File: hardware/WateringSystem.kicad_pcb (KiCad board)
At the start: 4 copper layers, 70 x 66 mm, 3 parts, among them IC1 MAX485ESA+T, U1 ESP32-DEVKITC-32E

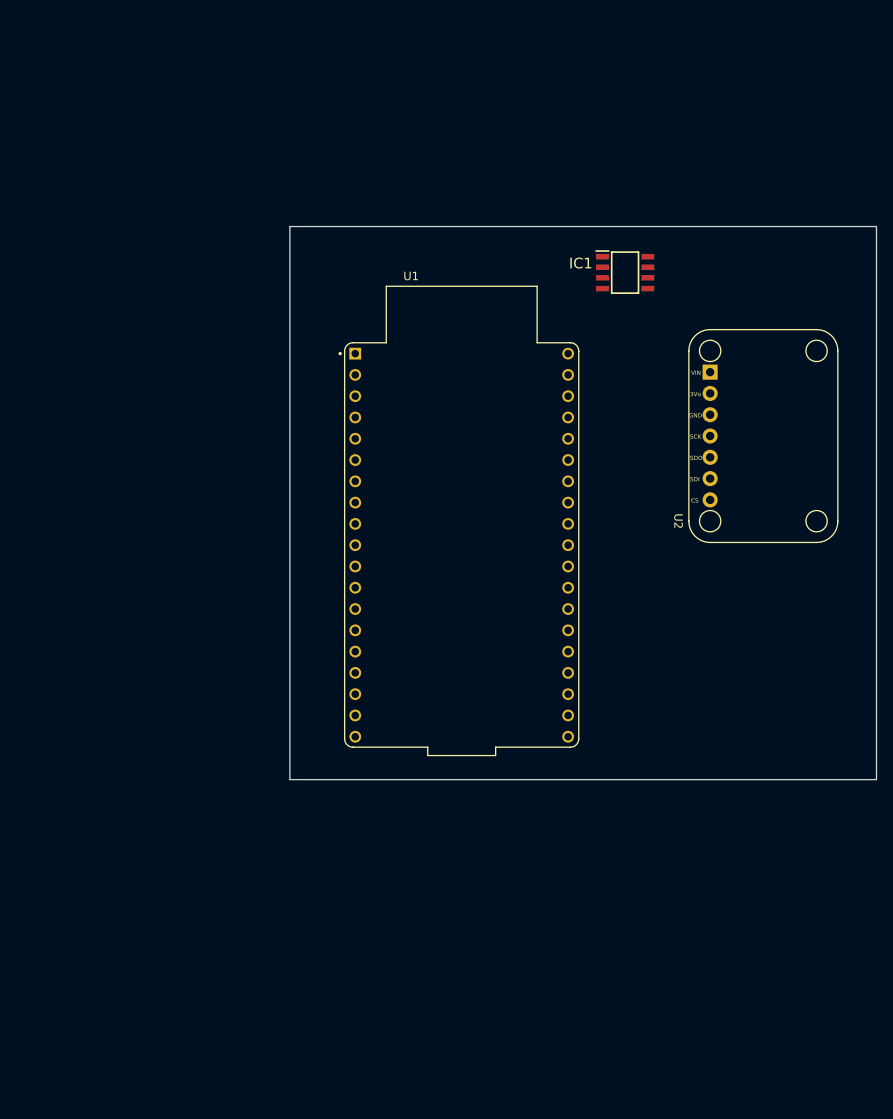
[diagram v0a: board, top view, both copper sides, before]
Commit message: Uppdaterat KiCad-schema med TXS0108E och nätlista
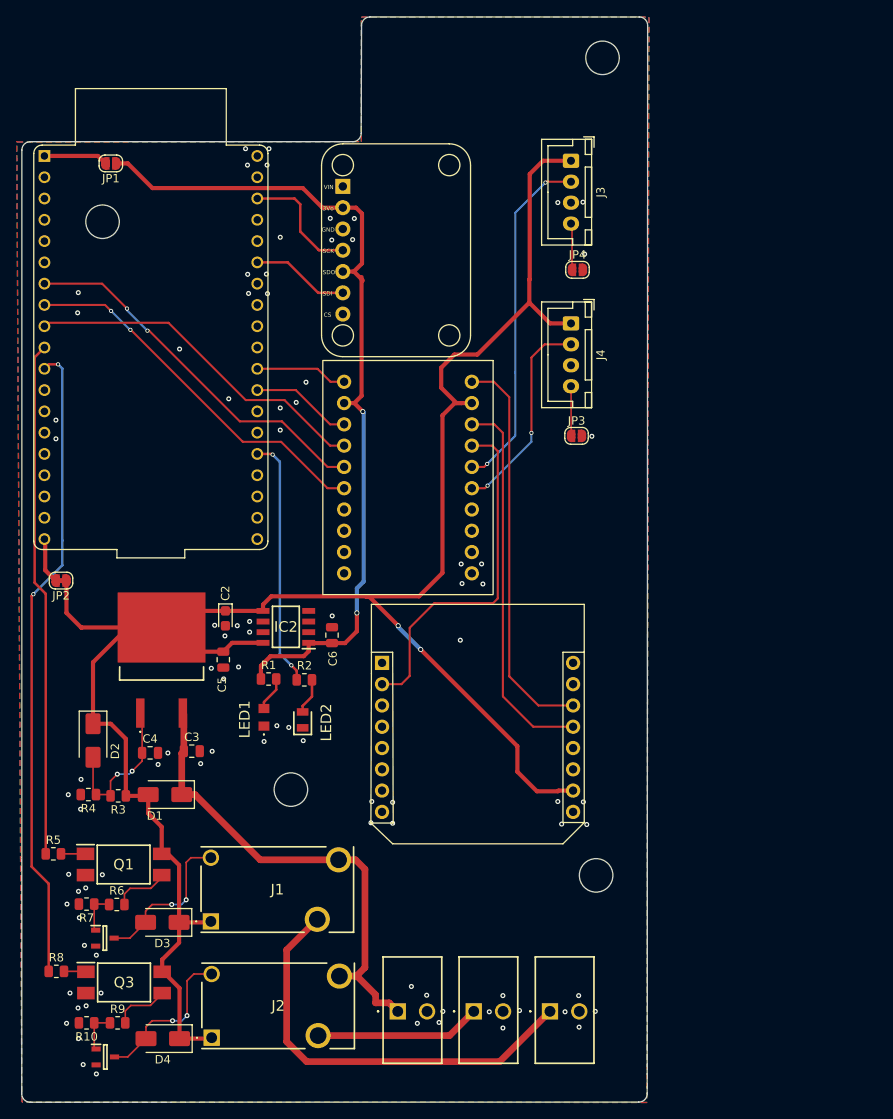
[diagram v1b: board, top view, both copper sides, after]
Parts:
- added Breakoutboard1: ~, Development_boards_custom:MAX485ESA+T_breakout, F.Cu at (131.4, 113.3)
- added C2: 1u, Capacitor_Tantalum_SMD:CP_EIA-2012-12_Kemet-R, F.Cu at (101.3, 109.3)
- added C3: 0u1, Capacitor_SMD:C_0805_2012Metric, F.Cu at (97.3, 125.1)
- added C4: 10u, Capacitor_SMD:C_0805_2012Metric, F.Cu at (92.3, 125.3)
- added C5: 10u, Capacitor_SMD:C_0805_2012Metric, F.Cu at (101.1, 114.2)
- added C6: 10u, Capacitor_SMD:C_0805_2012Metric, F.Cu at (114.0, 111.3)
- added D1: SS14, Diode_SMD:D_SMA, F.Cu at (94.1, 130.3)
- added D2: SS14, Diode_SMD:D_SMA, F.Cu at (85.5, 123.8)
- added D3: M7, Diode_SMD:D_SMA, F.Cu at (93.8, 145.5)
- added D4: M7, Diode_SMD:D_SMA, F.Cu at (93.8, 159.4)
- added H1: MountingHole, MountingHole:MountingHole_4mm, F.Cu at (86.6, 61.9)
- added H2: MountingHole, MountingHole:MountingHole_4mm, F.Cu at (146.3, 42.4)
- added H3: MountingHole, MountingHole:MountingHole_4mm, F.Cu at (109.1, 129.7)
- added H4: MountingHole, MountingHole:MountingHole_4mm, F.Cu at (145.5, 139.9)
- added IC2: AP2115M-3.3TRG1, Samacsys:SOIC127P600X175-8N, F.Cu at (108.5, 110.3)
- added J1: MAIN_PUMP_RELAY, Samacsys:120715561, F.Cu at (99.6, 145.4)
- added J2: RESERVOIR_PUMP_RELAY, Samacsys:120715561, F.Cu at (99.7, 159.3)
- added J3: RESERVOIR_SENSOR_LOW, Connector_JST:JST_XH_B4B-XH-A_1x04_P2.50mm_Vertical, F.Cu at (142.5, 54.6)
- added J4: RESERVOIR_SENSOR_HIGH, Connector_JST:JST_XH_B4B-XH-A_1x04_P2.50mm_Vertical, F.Cu at (142.5, 74.1)
- added J5: 12V_INPUT, Samacsys:WEID_1715010000, F.Cu at (121.9, 156.2)
- added J6: RESERVOIR_PUMP_OUT, Samacsys:WEID_1715010000, F.Cu at (130.9, 156.2)
- added J7: MAIN_PUMP_OUT, Samacsys:WEID_1715010000, F.Cu at (140.0, 156.2)
- added JP1: +3V3_open, Jumper:SolderJumper-2_P1.3mm_Open_RoundedPad1.0x1.5mm, F.Cu at (87.6, 55.0)
- added JP2: +5V_Closed, Jumper:SolderJumper-2_P1.3mm_Bridged_RoundedPad1.0x1.5mm, F.Cu at (81.7, 104.7)
- added JP3: normal_open, Jumper:SolderJumper-2_P1.3mm_Open_RoundedPad1.0x1.5mm, F.Cu at (143.2, 87.5)
- added JP4: normal_open, Jumper:SolderJumper-2_P1.3mm_Open_RoundedPad1.0x1.5mm, F.Cu at (143.3, 67.7)
- added LED1: PWR, Samacsys:150080SS75000, F.Cu at (105.9, 121.1)
- added LED2: STATUS, Samacsys:LEDC2012X80N, F.Cu at (110.5, 121.4)
- added Q1: FOD817BSD, Samacsys:SOP254P1016X385-4N, F.Cu at (89.2, 138.6)
- added Q2: SS8050-G, Samacsys:SOT95P240X115-3N, F.Cu at (86.9, 147.4)
- added Q3: FOD817BSD, Samacsys:SOP254P1016X385-4N, F.Cu at (89.2, 152.7)
- added Q4: SS8050-G, Samacsys:SOT95P240X115-3N, F.Cu at (87.0, 161.6)
- added R1: 100, Resistor_SMD:R_0805_2012Metric, F.Cu at (106.5, 116.5)
- added R10: 10k, Resistor_SMD:R_0805_2012Metric, F.Cu at (84.7, 157.5)
- added R2: 100, Resistor_SMD:R_0805_2012Metric, F.Cu at (110.7, 116.6)
- added R3: 240, Resistor_SMD:R_0805_2012Metric, F.Cu at (88.5, 130.4)
- added R4: 715, Resistor_SMD:R_0805_2012Metric, F.Cu at (84.9, 130.3)
- added R5: 100, Resistor_SMD:R_0805_2012Metric, F.Cu at (80.8, 137.4)
- added R6: 1k, Resistor_SMD:R_0805_2012Metric, F.Cu at (88.3, 143.4)
- added R7: 10k, Resistor_SMD:R_0805_2012Metric, F.Cu at (84.7, 143.4)
- added R8: 100, Resistor_SMD:R_0805_2012Metric, F.Cu at (81.1, 151.4)
- added R9: 1k, Resistor_SMD:R_0805_2012Metric, F.Cu at (88.4, 157.5)
- added U4: ~, Development_boards_custom:TXS10108E_breakout, F.Cu at (123.1, 93.7)
- IC1: value MAX485ESA+T -> LM317BD2TR4G; footprint Samacsys:SOIC127P600X175-8N -> Samacsys:LM317BD2TR4G
- U1: footprint Snapeda:ESP32-DEVKITC-32E_MODULE_ESP32-DEVKITC-32E -> Snapeda:ESP32-DEVKITC-32E_MODULE_ESP32-DEVKITC-32E-for headers
- moved IC1 71.9 mm to (93.7, 114.0)
- moved U2 49.1 mm to (121.7, 65.3)
- moved U1 44.0 mm to (92.4, 76.9)
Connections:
- IC1 pad 1: unconnected-(IC1-RO-Pad1) -> /ADJ
- IC1 pad 2: unconnected-(IC1-~{RE}-Pad2) -> +5V
- IC1 pad 3: unconnected-(IC1-DE-Pad3) -> +12V
- U1 pad J2_1: unconnected-(U1-3V3-PadJ2_1) -> /+3V3_C
- U1 pad J2_10: unconnected-(U1-IO26-PadJ2_10) -> /MAIN_PUMP_CONTROL
- U1 pad J2_11: unconnected-(U1-IO27-PadJ2_11) -> /RESERVOIR_PUMP_CONTROL
- U1 pad J2_14: unconnected-(U1-GND_J2_14-PadJ2_14) -> GND
- U1 pad J2_19: unconnected-(U1-EXT_5V-PadJ2_19) -> /+5V_C
- U1 pad J2_7: unconnected-(U1-IO32-PadJ2_7) -> /RESERVOIR_LOW_LEVEL_3V3
- U1 pad J2_8: unconnected-(U1-IO33-PadJ2_8) -> /RESERVOIR_HIGH_LEVEL_3V3
- U1 pad J2_9: unconnected-(U1-IO25-PadJ2_9) -> /RS485_DE_RE_3V3
- U1 pad J3_1: unconnected-(U1-GND_J3_1-PadJ3_1) -> GND
- U1 pad J3_10: unconnected-(U1-IO5-PadJ3_10) -> /BUTTON_MANUAL
- U1 pad J3_11: unconnected-(U1-IO17-PadJ3_11) -> /RS485_TX_3V3
- U1 pad J3_12: unconnected-(U1-IO16-PadJ3_12) -> /RS485_RX_3V3
- U1 pad J3_15: unconnected-(U1-IO2-PadJ3_15) -> /STATUS_LED
- U1 pad J3_3: unconnected-(U1-IO22-PadJ3_3) -> /I2C_SCL
- U1 pad J3_6: unconnected-(U1-IO21-PadJ3_6) -> /I2C_SDA
- U1 pad J3_7: unconnected-(U1-GND_J3_7-PadJ3_7) -> GND
- U1 pad J3_9: unconnected-(U1-IO18-PadJ3_9) -> /BUTTON_CONFIG
- U2 pad 2: unconnected-(U2-3Vo-Pad2) -> +3V3
- U2 pad 3: unconnected-(U2-GND-Pad3) -> GND
- U2 pad 4: unconnected-(U2-SCK-Pad4) -> /I2C_SCL
- U2 pad 5: unconnected-(U2-SDO-Pad5) -> +3V3
- U2 pad 6: unconnected-(U2-SDI-Pad6) -> /I2C_SDA
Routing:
- net +5V: track 0.00 -> 243.8 mm, vias 0 -> 2
- net +3V3: track 0.00 -> 102.0 mm, vias 0 -> 2
- net /RESERVOIR_PUMP_CONTROL: track 0.00 -> 77.3 mm, vias 0 -> 2
- net /MAIN_PUMP_CONTROL: track 0.00 -> 61.5 mm
- net +12V: track 0.00 -> 57.9 mm
- net /MAIN_PUMP_RELAY_CTRL: track 0.00 -> 51.0 mm
- net /RS485_TX_5V: track 0.00 -> 47.6 mm
- net /RS485_RX_5V: track 0.00 -> 45.5 mm
- net /RESERVOIR_LOW_LEVEL_3V3: track 0.00 -> 45.4 mm, vias 0 -> 2
- net /RESERVOIR_HIGH_LEVEL_3V3: track 0.00 -> 45.3 mm, vias 0 -> 2
- net /RS485_DE_RE_5V: track 0.00 -> 42.4 mm
- net /RS485_DE_RE_3V3: track 0.00 -> 41.7 mm
- net /RESERVOIR_LOW_LEVEL_5V: track 0.00 -> 41.5 mm, vias 0 -> 2
- net /STATUS_LED: track 0.00 -> 29.9 mm, vias 0 -> 2
- net /RESERVOIR_HIGH_LEVEL_5V: track 0.00 -> 24.8 mm, vias 0 -> 2
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- added copper zone on B.Cu, net GND
- added copper zone on F.Cu, net GND
- added copper zone on In1.Cu, net GND
- added copper zone on In2.Cu, net GND
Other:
- board size 70 x 66 mm -> 74.7 x 129.5 mm
- board text added: "${REFERENCE}"

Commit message: hardware: commit April design work — schematic pin fixes, PCB layout session, rev2 BOM (THVD1426), JLCPCB production files
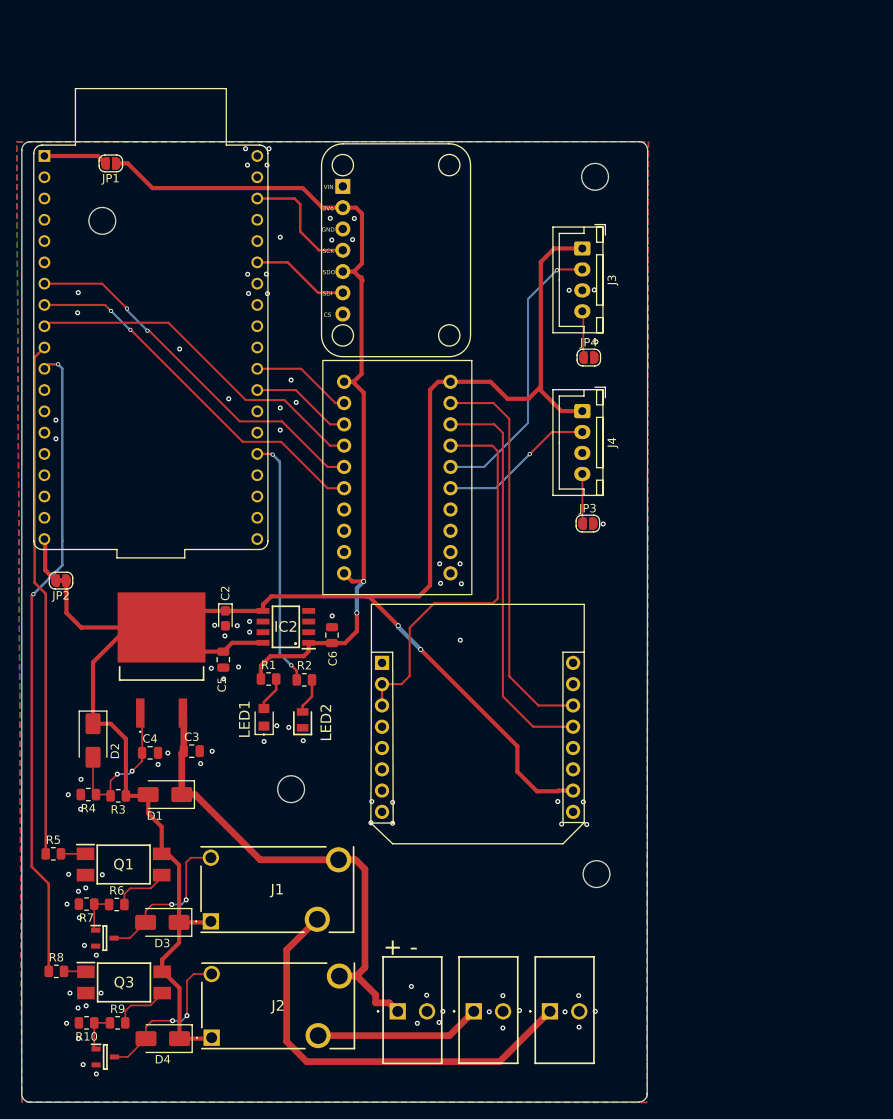
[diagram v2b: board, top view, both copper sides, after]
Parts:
- removed H1, H2, H3, H4: MountingHole, MountingHole:MountingHole_4mm
- added REF**: MountingHole_3.2mm_M3, MountingHole:MountingHole_3.2mm_M3, F.Cu at (145.4, 56.6)
- added REF**: MountingHole_3.2mm_M3, MountingHole:MountingHole_3.2mm_M3, F.Cu at (109.1, 129.6)
- added REF**: MountingHole_3.2mm_M3, MountingHole:MountingHole_3.2mm_M3, F.Cu at (86.6, 61.8)
- added REF**: MountingHole_3.2mm_M3, MountingHole:MountingHole_3.2mm_M3, F.Cu at (145.6, 139.8)
- moved JP3 10.6 mm to (144.6, 97.9)
- moved J4 10.6 mm to (143.9, 84.5)
- moved JP4 10.6 mm to (144.7, 78.1)
- moved J3 10.6 mm to (143.9, 65.1)
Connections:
- U4 pad 1: /RS485_TX_3V3 -> +3V3
- U4 pad 10: unconnected-(U4-OE-Pad10) -> +3V3
- U4 pad 19: +5V -> /RS485_TX_5V
- U4 pad 2: +3V3 -> /RS485_TX_3V3
- U4 pad 20: /RS485_TX_5V -> +5V
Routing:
- net /RESERVOIR_LOW_LEVEL_5V: track 41.5 -> 34.2 mm, vias 2 -> 1
- net /RESERVOIR_HIGH_LEVEL_5V: track 24.8 -> 18.5 mm, vias 2 -> 1
- net +5V: track 243.8 -> 237.9 mm
- net /RS485_DE_RE_5V: track 42.4 -> 47.4 mm
- net +3V3: track 102.0 -> 104.8 mm
- net /RS485_RX_5V: track 45.5 -> 48.0 mm
- net /RS485_TX_3V3: track 11.1 -> 11.6 mm
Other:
- board size 74.7 x 129.5 mm -> 74.7 x 114.6 mm
- board text added: "+ -"
- board text removed: "${REFERENCE}"
